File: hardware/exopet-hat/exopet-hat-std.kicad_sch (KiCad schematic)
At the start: 88 parts, among them J1 12V DC in, J10 CH3 12V OUT, J11 CH4 dry contact, J13 FLOAT1 switch, J14 FLOAT2 switch, J15 pH probe BNC, J3 RPi GPIO (HAT), J4 TEMP (3V3/DATA/GND), J8 CH1 12V OUT, J9 CH2 12V OUT, K1 G5LE-1-CF DC12, K2 G5LE-1-CF DC12, K3 G5LE-1-CF DC12, K4 G5LE-1-CF DC12, Q1 AOD403, U10 MCP6002 (pH buffers), U2 TBD62003AFG, U4 CAT24C32, U5 5V ESD clamp (SOD-323), U6 TPS54302DDC, U7 ADS1115 (floats, 0x48), U8 ADS1115 (pH, 0x49), U9 ISO1540 I2C isolator

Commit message: HAT: variant architecture — 'std' (65x56 HAT-compliant + float supervision) green
One parameterized source, two products: gen_schematic/gen_board/
preflight/golden/fab all take a variant (std|pro). std = the validated
rev-2 design + ADS1115 float-supervision ADC (0x48), 10k taps, and
I2C1 on J3 pins 3/5 — placed in the slots the debounce caps vacated;
detects no-sensor (3.3V) vs open (3.0V) vs closed (<0.3V) with EOL
resistors in the sensor plugs. Stays formally HAT-spec compliant.

Suffixed artifacts per variant (exopet-hat-std.*, fab/std/). Project
file now carries 0.15mm clearance rules (MSOP-10 pitch; JLC min is
0.127). DSN edge inset deepened to 0.45 to clear the 0.4 edge rule
structurally. GPIO23 pre-route rerouted clear of TP3 (its own true-
positive DRC catch). std preflight fully green: 73 parts, 228-pin
golden audit, DRC 0/0, fab cross-check 68 refs.

pro variant (isolated pH island, 65x70) has schematic + checkers ready;
board layout is the next step.

Co-Authored-By: Claude Fable 5 <noreply@anthropic.com>
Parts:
- removed C20, C21, C25: 100nF, Capacitor_SMD:C_0805_2012Metric, symbol Device:C
- removed C22: 10uF 10V, Capacitor_SMD:C_1206_3216Metric, symbol Device:C
- removed C26: 100nF (bias), Capacitor_SMD:C_0805_2012Metric, symbol Device:C
- removed C27: 4.7uF 25V, Capacitor_SMD:C_1206_3216Metric, symbol Device:C
- removed J15: pH probe BNC, Connector_Coaxial:BNC_Amphenol_031-6575_Horizontal, symbol Connector:Conn_Coaxial
- removed PS1: B0505S-1WR2 iso DC-DC (SIP-4), ExoPet:Converter_DCDC_B0505S-1W_SIP4, symbol Connector_Generic:Conn_01x04
- removed R24: 100k (bias hi), Resistor_SMD:R_0805_2012Metric, symbol Device:R
- removed R25: 100k (bias lo), Resistor_SMD:R_0805_2012Metric, symbol Device:R
- removed R26: 4.7k (iso SDA pullup), Resistor_SMD:R_0805_2012Metric, symbol Device:R
- removed R27: 4.7k (iso SCL pullup), Resistor_SMD:R_0805_2012Metric, symbol Device:R
- removed U10: MCP6002 (pH buffers), Package_SO:SOIC-8_3.9x4.9mm_P1.27mm, symbol Amplifier_Operational:MCP6002-xSN
- removed U8: ADS1115 (pH, 0x49), Package_SO:MSOP-10_3x3mm_P0.5mm, symbol Analog_ADC:ADS1115IDGS
- removed U9: ISO1540 I2C isolator, Package_SO:SOIC-8_3.9x4.9mm_P1.27mm, symbol Isolator:ISO1540
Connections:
- no-connect marks 27 -> 26

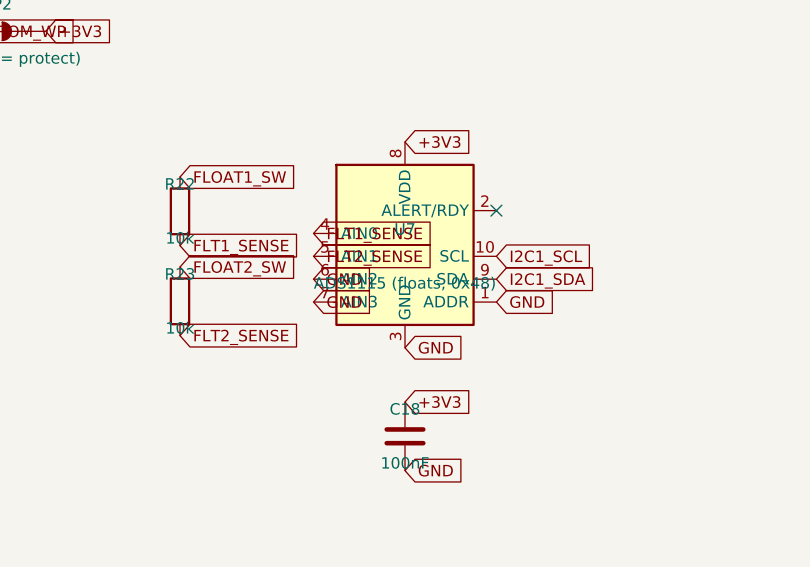
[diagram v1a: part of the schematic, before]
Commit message: HAT pro: expand to 6 relays + 2 more supervised sensor inputs (schematic)
Pro gains CH5 (switched 12V, GPIO24) + CH6 (dry contact, GPIO25) on the
existing TBD62003 driver (now 6/7 channels), each with the standard
fuse/flyback/terminal/LED per their type; and SW3/SW4 general
supervised switch inputs on the sensor ADC's spare A2/A3 channels
(ADC-only, 3-state EOL detection like the floats). J3 pins 18/22 carry
the new GPIO. All 6-relay/sensor parts are add_pro-gated so std stays a
4-relay 65x56 HAT-compliant board. add_pro hoisted above first use
(was NameError-crashing pro generation silently under suppressed
stderr). Both variants: ERC benign-only, golden + polarity clean
(pro-only refs conditionally gated). pro=117 parts, std=79. Board
layout (65x88, 2x3 relays) next.

Co-Authored-By: Claude Fable 5 <noreply@anthropic.com>
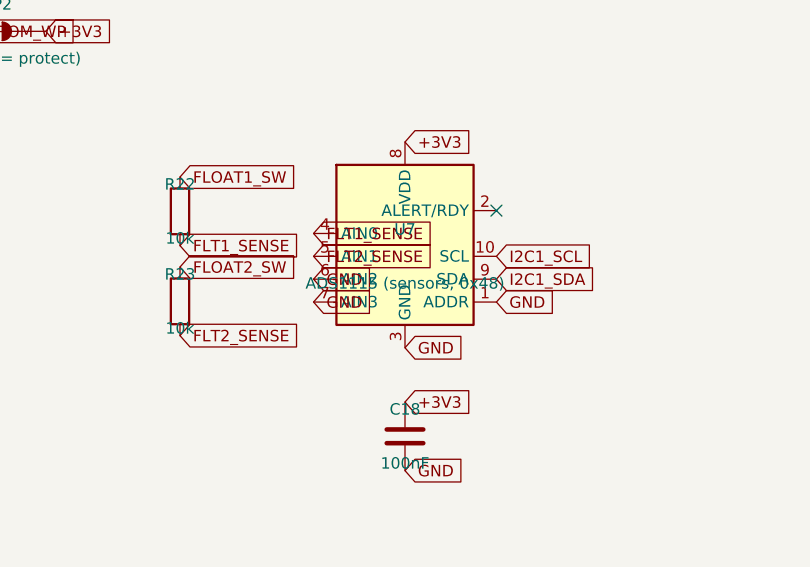
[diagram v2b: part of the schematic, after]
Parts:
- U7: value ADS1115 (floats, 0x48) -> ADS1115 (sensors, 0x48)
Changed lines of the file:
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@@
     (exclude_from_sim no) (in_bom yes) (on_board yes) (dnp no)
     (property "Reference" "U7" (at 240 197 0) (effects (font (size 1.27 1.27))))
-    (property "Value" "ADS1115 (floats, 0x48)" (at 240 203 0) (effects (font (size 1.27 1.27))))
+    (property "Value" "ADS1115 (sensors, 0x48)" (at 240 203 0) (effects (font (size 1.27 1.27))))
     (property "Footprint" "Package_SO:MSOP-10_3x3mm_P0.5mm" (at 240 200 0) (effects (font (size 1.27 1.27)) hide))
     (property "LCSC" "VERIFY" (at 240 200 0) (effects (font (size 1.27 1.27)) hide))
@@
   (no_connect (at 149.68 49.68))
   (no_connect (at 149.68 59.84))
-  (no_connect (at 149.68 80.16))
   (no_connect (at 190.32 80.16))
   (no_connect (at 190.32 77.62))
-  (no_connect (at 149.68 82.7))
   (no_connect (at 190.32 82.7))
   (no_connect (at 190.32 75.08))
@@
   (no_connect (at 149.68 67.46))
   (no_connect (at 149.68 70.0))
+  (no_connect (at 149.68 80.16))
+  (no_connect (at 149.68 82.7))
+  (no_connect (at 250.16 50.08))
+  (no_connect (at 250.16 52.62))
   (no_connect (at 250.16 55.16))
-  (no_connect (at 250.16 52.62))
-  (no_connect (at 250.16 50.08))
   (no_connect (at 292.54 32.38))
   (no_connect (at 292.54 72.38))

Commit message: HAT std: verified JLC part numbers + DFM hole-fit pass (13 blanks -> 3)
Researched & datasheet-verified LCSC codes filled for 9 lines (10uF
C14860, 22uF C309062, 100uF elec C3338, 12.7k C17434, 75pF C113832,
ADS1115 C37593, EEPROM 24LC32A C511262, SMBJ16CA C71870, TPS54302
C311983). Each confirmed against a fetched LCSC/JLC page for
value+package match.

DFM FIX (found by this pass): D3 was 'B550C' on a D_SMB footprint, but
B550C is SMC (DO-214AB) — it would NOT fit the SMB holes. Swapped to
SS56(LOWVF) C2891311, a genuine SMB (DO-214AA) 5A 60V schottky and a
JLC *Basic* part. std re-verified fully green.

Through-hole hole-fit check (all PASS): F1 MF-RG700 leads 0.81mm <
1.01mm hole; F2-F4 = C208481 (Bourns MF-R110, 0.51mm leads) < 0.71mm
hole; relays C1524650 match Omron's 1.3mm spec. The rev-1 fuse-leg
rejection cannot recur.

3 lines remain blank by necessity: J1 barrel jack (not in JLC assembly
lib), L1 inductor + F1 7A fuse (no fetch-confirmed LCSC code found —
NOT guessed; hints kept). F1 also needs a decision: MF-RG700 isn't
JLC-stocked and its body is taller than the RG500 footprint.

Co-Authored-By: Claude Fable 5 <noreply@anthropic.com>
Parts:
- C1: LCSC VERIFY -> C3338
- C11, C12: LCSC VERIFY -> C309062
- C16, C8: LCSC VERIFY -> C14860
- C17: LCSC VERIFY -> C113832
- D1: LCSC VERIFY -> C71870
- D3: value B550C 5A 30V (5V safety diode) -> SS56 5A 60V (5V safety diode, SMB); LCSC VERIFY -> C2891311
- R17: LCSC VERIFY -> C17434
- U4: LCSC VERIFY -> C511262
- U6: LCSC VERIFY -> C311983
- U7: LCSC VERIFY -> C37593
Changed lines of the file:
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@@
     (property "Value" "SMBJ16CA bidirectional" (at 55 63 0) (effects (font (size 1.27 1.27))))
     (property "Footprint" "Diode_SMD:D_SMB" (at 55 60 0) (effects (font (size 1.27 1.27)) hide))
-    (property "LCSC" "VERIFY" (at 55 60 0) (effects (font (size 1.27 1.27)) hide))
+    (property "LCSC" "C71870" (at 55 60 0) (effects (font (size 1.27 1.27)) hide))
     (pin "1")
     (pin "2")
@@
     (property "Value" "10uF 25V X7R 1206" (at 105 43 0) (effects (font (size 1.27 1.27))))
     (property "Footprint" "Capacitor_SMD:C_1206_3216Metric" (at 105 40 0) (effects (font (size 1.27 1.27)) hide))
-    (property "LCSC" "VERIFY" (at 105 40 0) (effects (font (size 1.27 1.27)) hide))
+    (property "LCSC" "C14860" (at 105 40 0) (effects (font (size 1.27 1.27)) hide))
     (pin "1")
     (pin "2")
@@
     (property "Value" "100uF 25V SMD electrolytic 6.3x7.7" (at 120 43 0) (effects (font (size 1.27 1.27))))
     (property "Footprint" "Capacitor_SMD:CP_Elec_6.3x7.7" (at 120 40 0) (effects (font (size 1.27 1.27)) hide))
-    (property "LCSC" "VERIFY" (at 120 40 0) (effects (font (size 1.27 1.27)) hide))
+    (property "LCSC" "C3338" (at 120 40 0) (effects (font (size 1.27 1.27)) hide))
     (pin "1")
     (pin "2")
@@
     (property "Value" "TPS54302DDC" (at 30 93 0) (effects (font (size 1.27 1.27))))
     (property "Footprint" "Package_TO_SOT_SMD:SOT-23-6" (at 30 90 0) (effects (font (size 1.27 1.27)) hide))
-    (property "LCSC" "VERIFY" (at 30 90 0) (effects (font (size 1.27 1.27)) hide))
+    (property "LCSC" "C311983" (at 30 90 0) (effects (font (size 1.27 1.27)) hide))
     (pin "1")
     (pin "2")
@@
     (property "Value" "10uF 25V X7R 1206" (at 95 88 0) (effects (font (size 1.27 1.27))))
     (property "Footprint" "Capacitor_SMD:C_1206_3216Metric" (at 95 85 0) (effects (font (size 1.27 1.27)) hide))
-    (property "LCSC" "VERIFY" (at 95 85 0) (effects (font (size 1.27 1.27)) hide))
+    (property "LCSC" "C14860" (at 95 85 0) (effects (font (size 1.27 1.27)) hide))
     (pin "1")
     (pin "2")
@@
     (property "Value" "22uF 25V X7R 1210" (at 95 103 0) (effects (font (size 1.27 1.27))))
     (property "Footprint" "Capacitor_SMD:C_1210_3225Metric" (at 95 100 0) (effects (font (size 1.27 1.27)) hide))
-    (property "LCSC" "VERIFY" (at 95 100 0) (effects (font (size 1.27 1.27)) hide))
+    (property "LCSC" "C309062" (at 95 100 0) (effects (font (size 1.27 1.27)) hide))
     (pin "1")
     (pin "2")
@@
     (property "Value" "22uF 25V X7R 1210" (at 110 103 0) (effects (font (size 1.27 1.27))))
     (property "Footprint" "Capacitor_SMD:C_1210_3225Metric" (at 110 100 0) (effects (font (size 1.27 1.27)) hide))
-    (property "LCSC" "VERIFY" (at 110 100 0) (effects (font (size 1.27 1.27)) hide))
+    (property "LCSC" "C309062" (at 110 100 0) (effects (font (size 1.27 1.27)) hide))
     (pin "1")
     (pin "2")
@@
     (property "Value" "12.7k (FB lo -> 5.29V pre-diode)" (at 90 113 0) (effects (font (size 1.27 1.27))))
     (property "Footprint" "Resistor_SMD:R_0805_2012Metric" (at 90 110 0) (effects (font (size 1.27 1.27)) hide))
-    (property "LCSC" "VERIFY" (at 90 110 0) (effects (font (size 1.27 1.27)) hide))
+    (property "LCSC" "C17434" (at 90 110 0) (effects (font (size 1.27 1.27)) hide))
     (pin "1")
     (pin "2")
@@
     (property "Value" "75pF C0G (feedforward, TI Table 7-2)" (at 105 113 0) (effects (font (size 1.27 1.27))))
     (property "Footprint" "Capacitor_SMD:C_0805_2012Metric" (at 105 110 0) (effects (font (size 1.27 1.27)) hide))
-    (property "LCSC" "VERIFY" (at 105 110 0) (effects (font (size 1.27 1.27)) hide))
+    (property "LCSC" "C113832" (at 105 110 0) (effects (font (size 1.27 1.27)) hide))
     (pin "1")
     (pin "2")
@@
     (exclude_from_sim no) (in_bom yes) (on_board yes) (dnp no)
     (property "Reference" "D3" (at 55 87 0) (effects (font (size 1.27 1.27))))
-    (property "Value" "B550C 5A 30V (5V safety diode)" (at 55 93 0) (effects (font (size 1.27 1.27))))
+    (property "Value" "SS56 5A 60V (5V safety diode, SMB)" (at 55 93 0) (effects (font (size 1.27 1.27))))
     (property "Footprint" "Diode_SMD:D_SMB" (at 55 90 0) (effects (font (size 1.27 1.27)) hide))
-    (property "LCSC" "VERIFY" (at 55 90 0) (effects (font (size 1.27 1.27)) hide))
+    (property "LCSC" "C2891311" (at 55 90 0) (effects (font (size 1.27 1.27)) hide))
     (pin "1")
     (pin "2")
@@
     (property "Value" "CAT24C32" (at 150 163 0) (effects (font (size 1.27 1.27))))
     (property "Footprint" "Package_SO:SOIC-8_3.9x4.9mm_P1.27mm" (at 150 160 0) (effects (font (size 1.27 1.27)) hide))
-    (property "LCSC" "VERIFY" (at 150 160 0) (effects (font (size 1.27 1.27)) hide))
+    (property "LCSC" "C511262" (at 150 160 0) (effects (font (size 1.27 1.27)) hide))
     (pin "1")
     (pin "2")
@@
     (property "Value" "ADS1115 (sensors, 0x48)" (at 240 203 0) (effects (font (size 1.27 1.27))))
     (property "Footprint" "Package_SO:MSOP-10_3x3mm_P0.5mm" (at 240 200 0) (effects (font (size 1.27 1.27)) hide))
-    (property "LCSC" "VERIFY" (at 240 200 0) (effects (font (size 1.27 1.27)) hide))
-    (pin "1")
-    (pin "2")
+    (property "LCSC" "C37593" (at 240 200 0) (effects (font (size 1.27 1.27)) hide))
+    (pin "1")
+    (pin "2")

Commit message: HAT std: AUX dry-contact gets the big 5.08mm terminal (14 AWG)
std's AUX (CH4, J11) -> KF301-5.0 (5.08mm, up to 14 AWG, C474882),
matched to the 10A relay contact. Switched channels CH1-3 stay 3.5mm
(fused 1A). To fit the wider AUX on the packed 65x56 front edge, the
four channel-state LEDs move to the back (rev-1 style) -- a deliberate
trade the user accepted (terminal prioritized over front LED
visibility). flip_backs is now variant-aware (std backs the LEDs; pro
keeps them top). Dry-contact codes variant-independent; switched-
channel codes variant-keyed. std fully green.

Co-Authored-By: Claude Fable 5 <noreply@anthropic.com>
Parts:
- J11: footprint TerminalBlock_Phoenix:TerminalBlock_Phoenix_PT-1,5-3-3.5-H_1x03_P3.50mm_Horizontal -> TerminalBlock_CUI:TerminalBlock_CUI_TB007-508-03_1x03_P5.08mm_Horizontal
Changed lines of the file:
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@@
     (property "Reference" "J11" (at 340 157 0) (effects (font (size 1.27 1.27))))
     (property "Value" "CH4 dry contact" (at 340 163 0) (effects (font (size 1.27 1.27))))
-    (property "Footprint" "TerminalBlock_Phoenix:TerminalBlock_Phoenix_PT-1,5-3-3.5-H_1x03_P3.50mm_Horizontal" (at 340 160 0) (effects (font (size 1.27 1.27)) hide))
+    (property "Footprint" "TerminalBlock_CUI:TerminalBlock_CUI_TB007-508-03_1x03_P5.08mm_Horizontal" (at 340 160 0) (effects (font (size 1.27 1.27)) hide))
     (property "LCSC" "" (at 340 160 0) (effects (font (size 1.27 1.27)) hide))
     (pin "1")
